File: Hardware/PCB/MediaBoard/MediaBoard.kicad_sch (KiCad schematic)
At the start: 35 parts

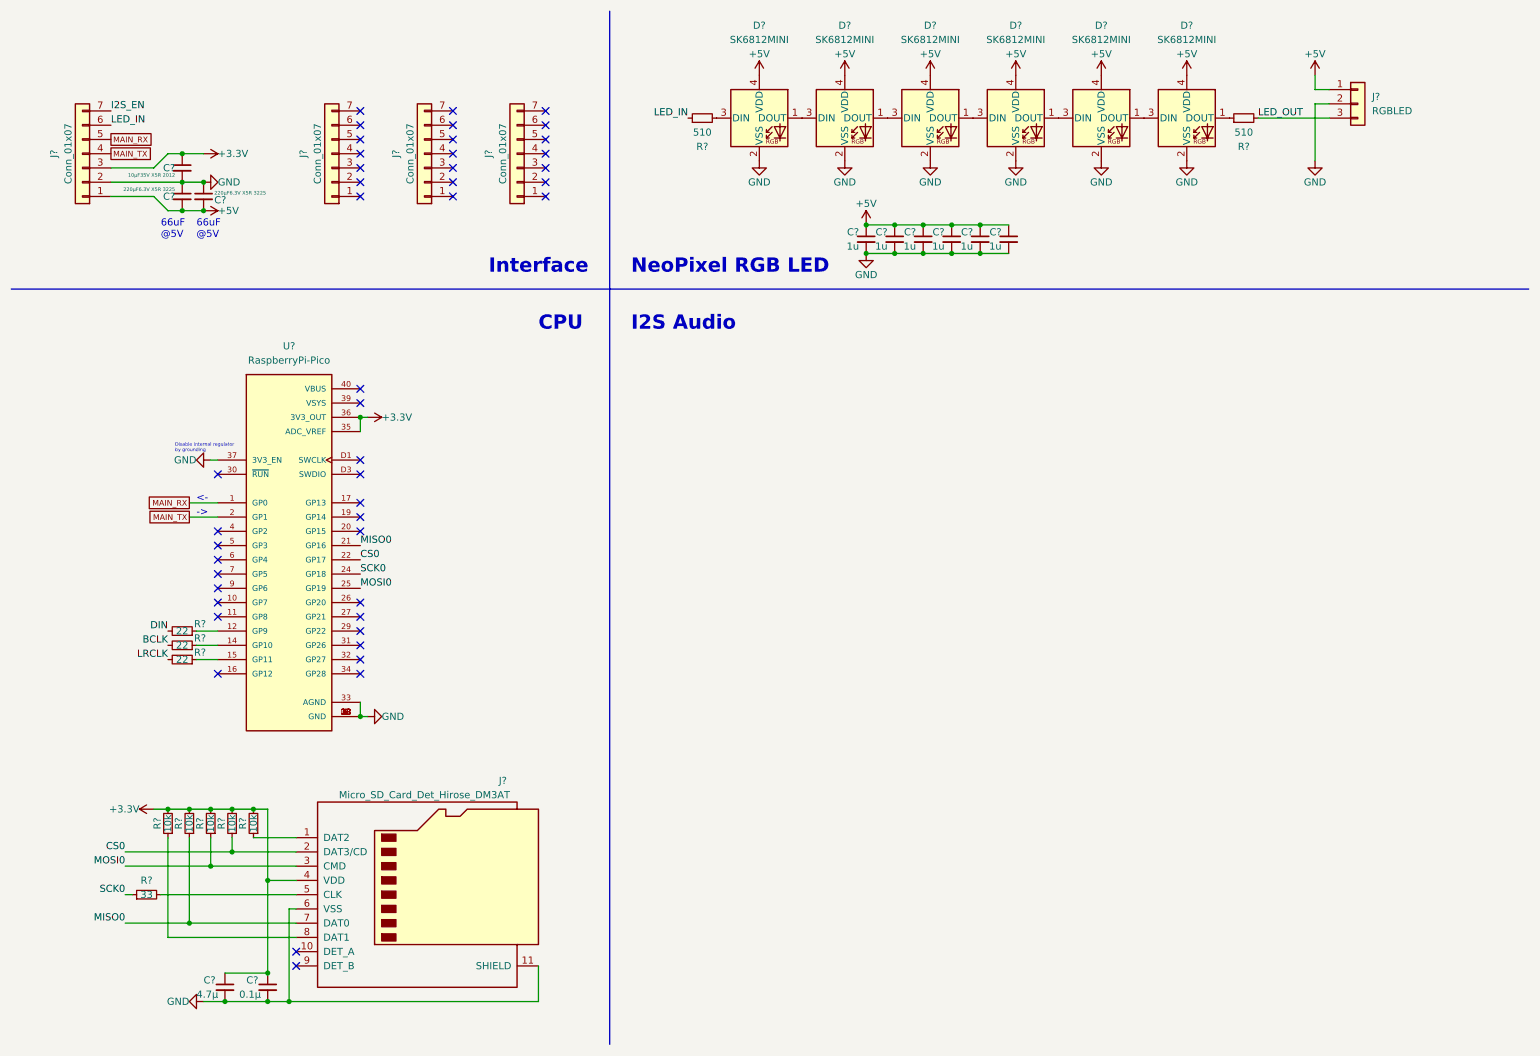
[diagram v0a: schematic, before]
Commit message: WisdPi_Tiny_RP2040のシンボル/フットプリントを作成
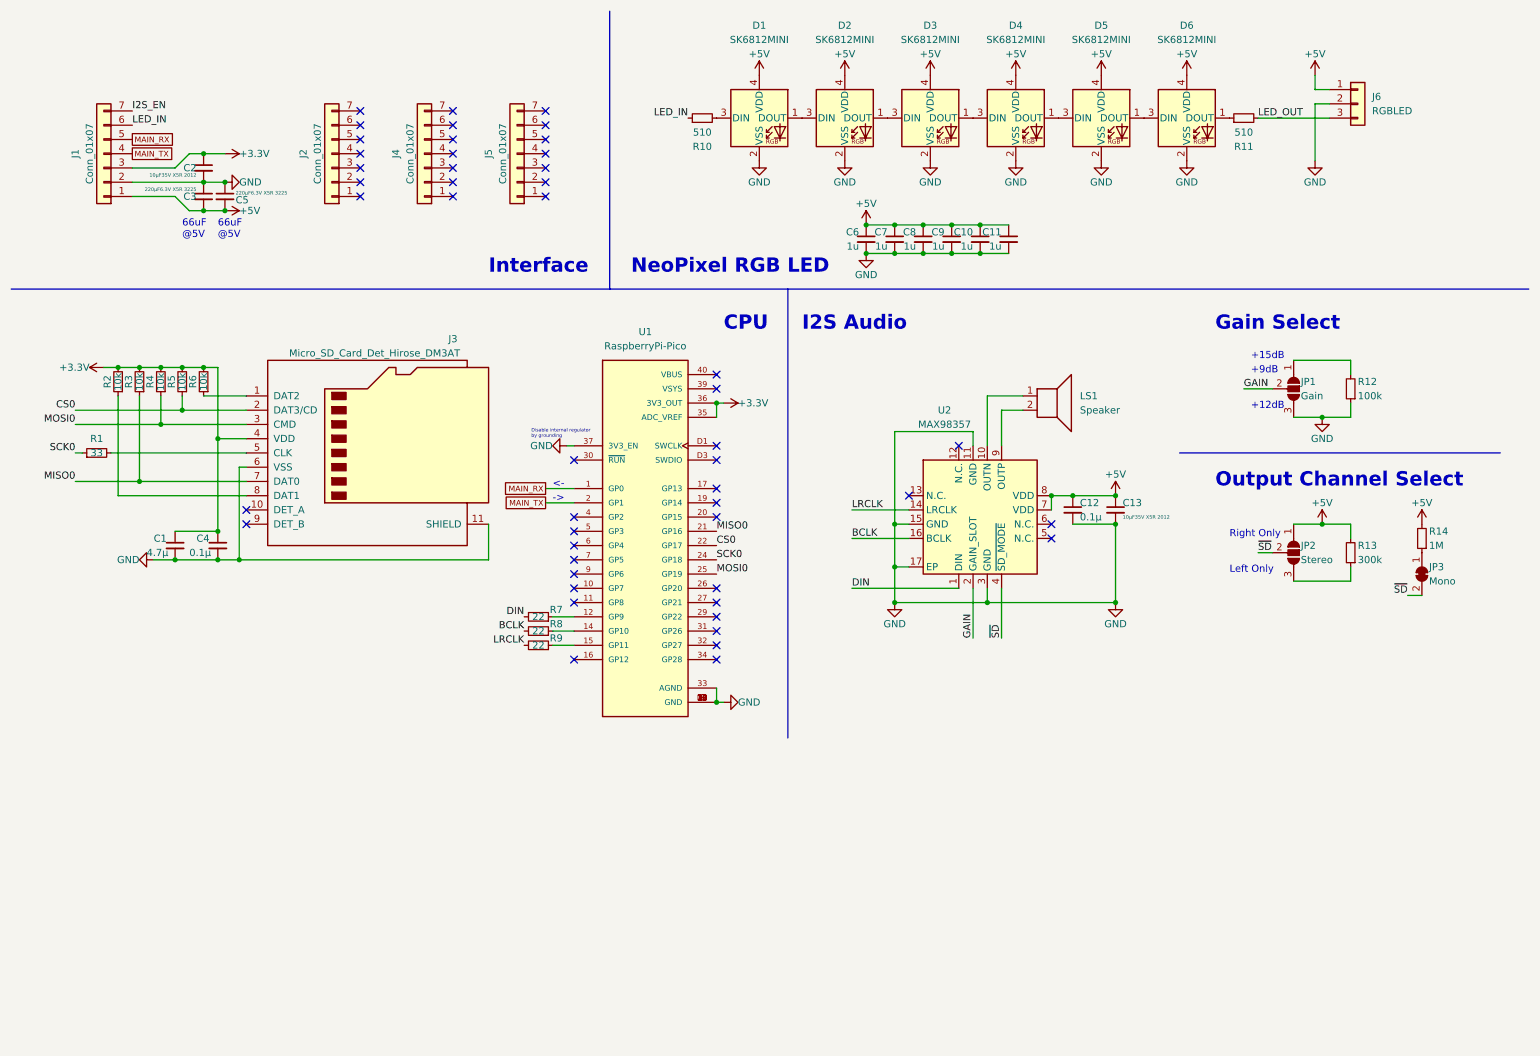
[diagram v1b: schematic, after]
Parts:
- added C12: 0.1μ, Capacitor_SMD:C_0603_1608Metric, symbol Device:C_Small
- added C13: 10μF35V X5R 2012, Capacitor_SMD:C_0805_2012Metric, symbol Device:C_Small
- added JP1: Gain, Jumper:SolderJumper-3_P1.3mm_Open_RoundedPad1.0x1.5mm, symbol Jumper:SolderJumper_3_Open
- added JP2: Stereo, Jumper:SolderJumper-3_P1.3mm_Open_RoundedPad1.0x1.5mm, symbol Jumper:SolderJumper_3_Open
- added JP3: Mono, Jumper:SolderJumper-2_P1.3mm_Bridged_RoundedPad1.0x1.5mm, symbol Jumper:SolderJumper_2_Bridged
- added LS1: Speaker, Connector_JST:JST_PH_S2B-PH-K_1x02_P2.00mm_Horizontal, symbol Device:Speaker
- added R12: 100k, Resistor_SMD:R_0603_1608Metric, symbol Device:R_Small
- added R13: 300k, Resistor_SMD:R_0603_1608Metric, symbol Device:R_Small
- added R14: 1M, Resistor_SMD:R_0603_1608Metric, symbol Device:R_Small
- added U2: MAX98357, Package_DFN_QFN:TQFN-16-1EP_3x3mm_P0.5mm_EP1.23x1.23mm_ThermalVias, symbol Amplifier_Audio_extlib:MAX98357
- C1, C4: renamed from C?; footprint Capacitor_SMD:C_0603_1608Metric_Pad1.08x0.95mm_HandSolder -> Capacitor_SMD:C_0603_1608Metric
- J6: renamed from J?; footprint (none) -> Connector_JST:JST_PH_S3B-PH-K_1x03_P2.00mm_Horizontal
- R1, R2, R3, R4, R5, R6, R7, R8, R9: renamed from R?; footprint Resistor_SMD:R_0603_1608Metric_Pad0.98x0.95mm_HandSolder -> Resistor_SMD:R_0603_1608Metric
- U1: renamed from U?; footprint (none) -> Module_extlib:RaspberryPi-Pico
- gave numbers to parts that had none: 22
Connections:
- net +5V: now also C12.1, C13.1, JP2.1 (A), R13.2, R14.2, U2.7 (VDD), U2.8 (VDD)
- net BCLK: now also U2.16 (BCLK)
- net DIN: now also U2.1 (DIN)
- net GND: now also C12.2, C13.2, JP1.3 (B), R12.1, U2.11 (GND), U2.15 (GND), U2.17 (EP), U2.3 (GND)
- net LRCLK: now also U2.14 (LRCLK)
- new net: LS1.1, U2.10 (OUTN)
- new net: LS1.2, U2.9 (OUTP)
- new net: JP2.3 (B), R13.1
- new net: JP3.1 (A), R14.1
- new net: JP1.1 (A), R12.2
- new net GAIN: JP1.2 (C), U2.2 (GAIN_SLOT)
- new net ~{SD}: JP2.2 (C), JP3.2 (B), U2.4 (~{SD_MODE})
- no-connect marks 45 -> 49
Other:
- note added: "+12dB"
- note added: "+15dB"
- note added: "+9dB"
- note added: "Gain Select"
- note added: "Left Only"
- note added: "Output Channel Select"
- note added: "Right Only"
- moved on the sheet: C1, C2, C3, C4, C5, J1, J3, R1, R2, R3, R4, R5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

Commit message: もろもろ更新
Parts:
- removed U1: RaspberryPi-Pico, Module_extlib:RaspberryPi-Pico, symbol MCU_Module_extlib:RaspberryPi-Pico
- added U1: WisdPi_Tiny_RP2040, Module_extlib:WisdPi_Tiny_RP2040, symbol MCU_Module_extlib:WisdPi_Tiny_RP2040
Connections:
- net +3.3V: now also U1.27 (3V3)
- net CS0: now also U1.18 (GP17)
- net GND: now also U1.28 (GND)
- net MAIN_RX: now also U1.1 (GP0)
- net MAIN_TX: now also U1.2 (GP1)
- net MISO0: now also U1.17 (GP16)
- net MOSI0: now also U1.20 (GP19)
- net SCK0: now also U1.19 (GP18)
- net at R9.1: now also U1.12 (GP11)
- net at R8.1: now also U1.11 (GP10)
- net at R7.1: now also U1.10 (GP9)
- no-connect marks 49 -> 45
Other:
- note removed: "Disable internal regulator by grounding"
- moved on the sheet: R7, R8, R9
